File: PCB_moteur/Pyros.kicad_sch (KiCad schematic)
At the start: 51 parts, among them J1 Screw_Terminal_01x08, U12 SI5442DU-T1-GE3, U3 SI5442DU-T1-GE3, U6 LM339, U7 SI5442DU-T1-GE3

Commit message: wip: change 4 pyros -> 2 pyros
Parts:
- removed J1: Screw_Terminal_01x08, ODB:8pin_terminal_2mm54, symbol Connector:Screw_Terminal_01x08
- removed P_C4, P_C8: 22uF, Capacitor_SMD:C_0603_1608Metric, symbol Device:C_Small
- removed P_C5, P_C9: 0.1uF, Capacitor_SMD:C_0603_1608Metric, symbol Device:C_Small
- removed P_D3, P_D4, P_D7, P_D8: CDBQR0230R, Diode_SMD:D_SOD-923, symbol Diode:BAT54J
- removed P_R10, P_R18: 27k, Resistor_SMD:R_0603_1608Metric, symbol Device:R_Small
- removed P_R11, P_R19: 100, Resistor_SMD:R_0603_1608Metric, symbol Device:R_Small
- removed P_R12, P_R20: 3.3k, Resistor_SMD:R_0603_1608Metric, symbol Device:R_Small
- removed P_R17, P_R9: 180k, Resistor_SMD:R_0603_1608Metric, symbol Device:R_Small
- removed U12, U3: SI5442DU-T1-GE3, SON_8DU-T1-GE3_VIS, symbol ODB2:SI5442DU-T1-GE3
- removed U6: LM339, Package_SO:TSSOP-14_4.4x5mm_P0.65mm, symbol Comparator:LM339
- added J1: Screw_Terminal_01x04, symbol Connector:Screw_Terminal_01x04
- added U8: LM393, symbol Comparator:LM393
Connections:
- net +5V: now also U8.8 (V+)
- net Cmp_1: now also U8.1
- net Cmp_2: now also U8.7
- net GND: now also U8.4 (V-)
- net Pyro1-: now also J1.2 (Pin_2)
- net Pyro2-: now also J1.4 (Pin_4)
- net Vin_Pyro: now also J1.1 (Pin_1), J1.3 (Pin_3)
- net at P_R2.2, P_R4.1: now also U8.2 (-), U8.6 (-)
- net at P_R1.2, P_R3.1: now also U8.3 (+), U8.5 (+)
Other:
- note removed: "Pyro 3"
- note removed: "Pyro 4"
- moved on the sheet: P_C1

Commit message: fix: power supply + add LED RG + add mounting holes + change 6pins header SWD connector + pyros
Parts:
- P_C2, P_C7: value 0.1uF -> 100nF
- P_R1: value 24k 1% -> 102k 1%
- P_R13, P_R5: value 180k -> 39k
- P_R14, P_R6: value 27k -> 22k
- P_R15, P_R7: value 100 -> 100R
- P_R2: value 20k 1% -> 40k 1%
- P_R3: value 3.6k 1% -> 10k 1%
- P_R4: value 5k 1% -> 10k 1%
- Vin_R3: value 27K 1% -> 22K 1%
- Vin_R4: value 180k 1% -> 39k 1%
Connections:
- net +5V is gone; now on net +3V3: P_C1.1, U8.8 (V+)
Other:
- note added: "Power good protection, block the ignition if the power is not above 7.4v if V_{in} > 7.4 = Power good V_{ref} = 3.3 * R4 / (R2 + R4) = 0.66V if V_{in} = 7.4 * R3 / (R3 + R1) = 0.66v"
- note removed: "2 colors availabel for the connector 1715250000 : Black 1715310000 : Orange"
- note removed: "Power good protection, block the ignition if the power is not above 5.06v if V_{in} > 5.06 = Power good V_{ref} = ${/4b06c5d1-aa8b-48ed-8972-b43a60cfab78/8ab7427e-7183-4caa-ac8a-08b0bd412372/a7ab30b6-1c68-4176-964a-109ef5b035cc:VALUE} * ${/4b06c5d1-aa8b-48ed-8972-b43a60cfab78/8ab7427e-7183-4caa-ac8a-08b0bd412372/0614f46a-a67b-4246-947a-398bbcc78170:VALUE} / (${/4b06c5d1-aa8b-48ed-8972-b43a60cfab7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"
- moved on the sheet: J1, P_C2, P_C3, P_C6, P_C7, P_D1, P_D2, P_D5, P_D6, P_R13, P_R14, P_R15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

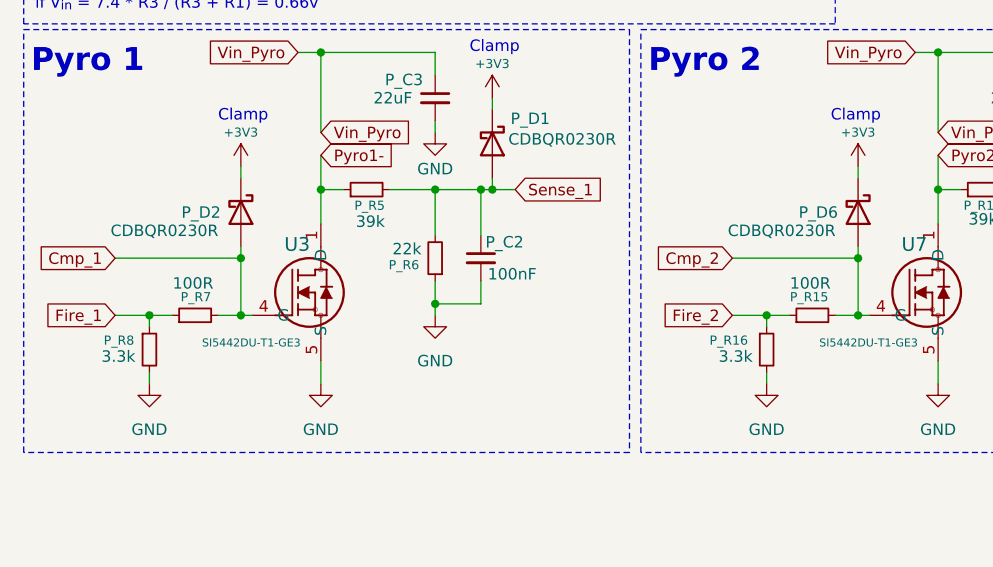
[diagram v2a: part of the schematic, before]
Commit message: fix: resistors + capacitances power supply
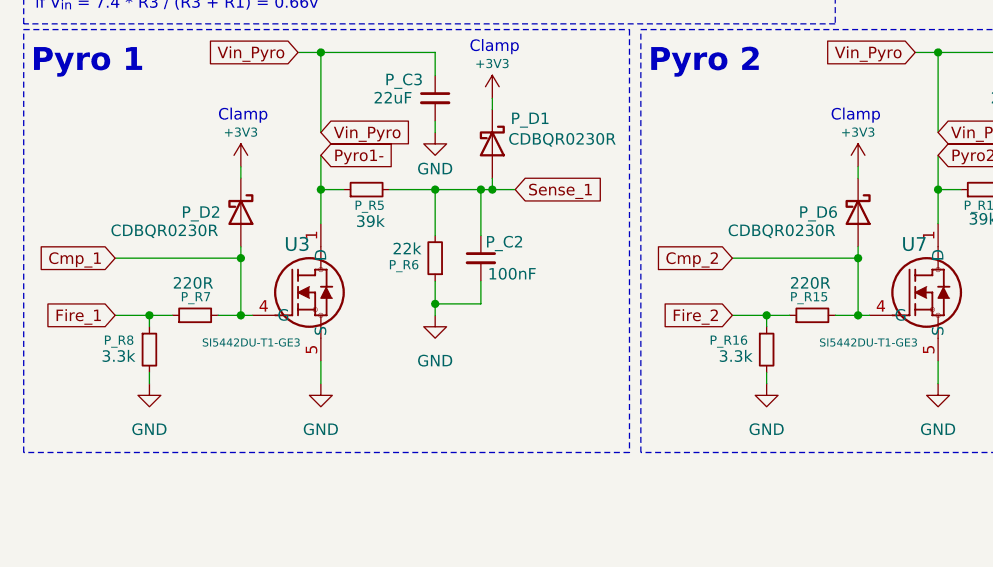
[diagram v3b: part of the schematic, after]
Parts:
- P_R15, P_R7: value 100R -> 220R
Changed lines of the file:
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@@
 			)
 		)
-		(property "Value" "100R"
+		(property "Value" "220R"
 			(at 103.632 112.014 90)
 			(effects
@@
 			)
 		)
-		(property "Value" "100R"
+		(property "Value" "220R"
 			(at 35.052 112.014 90)
 			(effects

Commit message: fix: pyros resistors + typos +
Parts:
- P_R15, P_R7: value 220R -> 1.5k
- P_R16, P_R8: value 3.3k -> 27k
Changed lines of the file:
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@@
 			)
 		)
-		(property "Value" "220R"
+		(property "Value" "1.5k"
 			(at 103.632 112.014 90)
 			(effects
@@
 			)
 		)
-		(property "Value" "3.3k"
+		(property "Value" "27k"
 			(at 22.606 120.142 0)
 			(effects
@@
 			)
 		)
-		(property "Value" "3.3k"
+		(property "Value" "27k"
 			(at 91.186 120.142 0)
 			(effects
@@
 			)
 		)
-		(property "Value" "220R"
+		(property "Value" "1.5k"
 			(at 35.052 112.014 90)
 			(effects

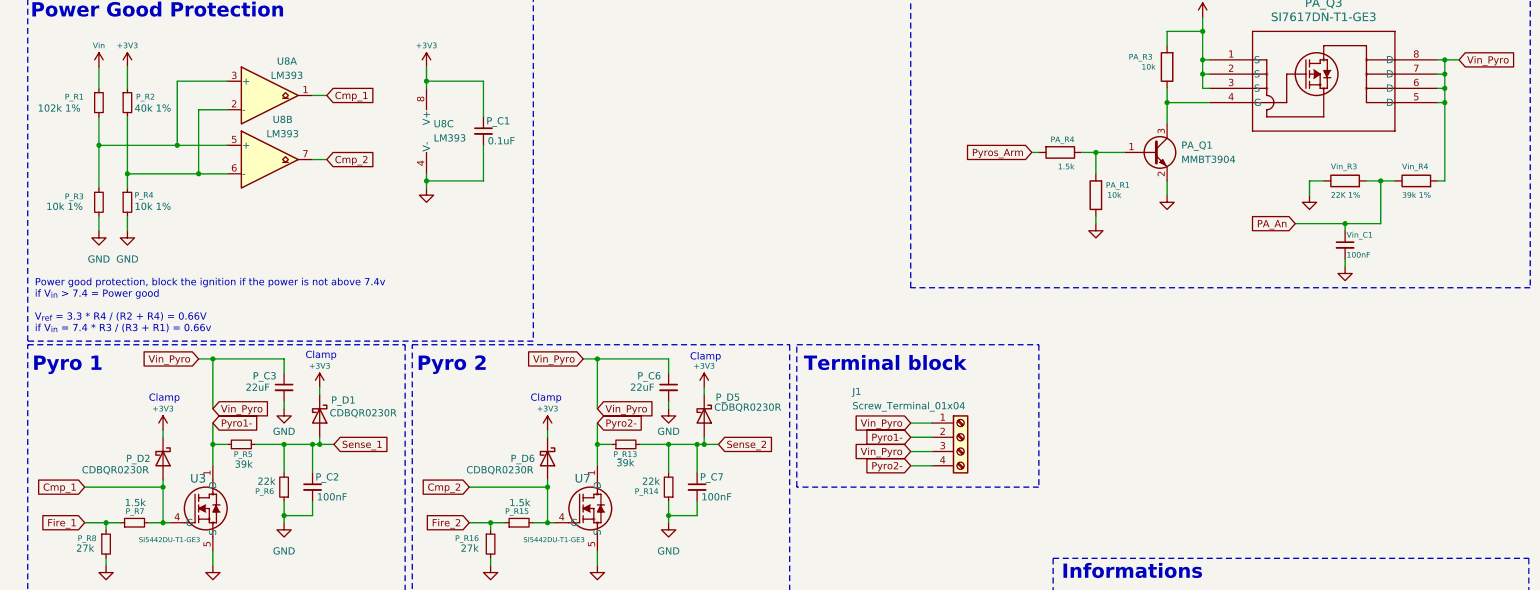
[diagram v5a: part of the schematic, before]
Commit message: fix: resistance ratios + typos
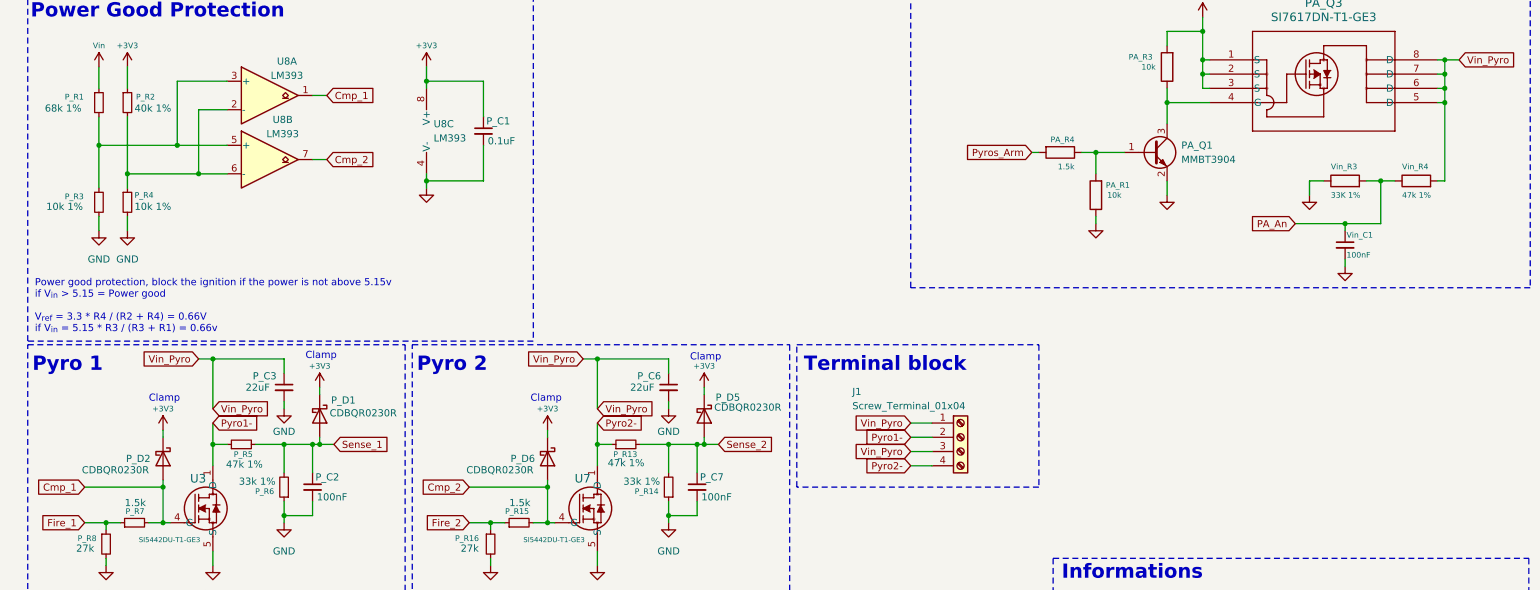
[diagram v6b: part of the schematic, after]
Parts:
- P_R1: value 102k 1% -> 68k 1%
- P_R13, P_R5: value 39k -> 47k 1%
- P_R14, P_R6: value 22k -> 33k 1%
- Vin_R3: value 22K 1% -> 33K 1%
- Vin_R4: value 39k 1% -> 47k 1%
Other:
- note added: "Power good protection, block the ignition if the power is not above 5.15v if V_{in} > 5.15 = Power good V_{ref} = 3.3 * R4 / (R2 + R4) = 0.66V if V_{in} = 5.15 * R3 / (R3 + R1) = 0.66v"
- note removed: "Power good protection, block the ignition if the power is not above 7.4v if V_{in} > 7.4 = Power good V_{ref} = 3.3 * R4 / (R2 + R4) = 0.66V if V_{in} = 7.4 * R3 / (R3 + R1) = 0.66v"
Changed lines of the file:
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@@
 		)
 	)
-	(text "Power good protection, block the ignition if the power is not above 7.4v\nif V_{in} > 7.4 = Power good\n\nV_{ref} = 3.3 * R4 / (R2 + R4) = 0.66V\nif V_{in} = 7.4 * R3 / (R3 + R1) = 0.66v\n"
+	(text "Power good protection, block the ignition if the power is not above 5.15v\nif V_{in} > 5.15 = Power good\n\nV_{ref} = 3.3 * R4 / (R2 + R4) = 0.66V\nif V_{in} = 5.15 * R3 / (R3 + R1) = 0.66v\n"
 		(exclude_from_sim no)
 		(at 15.24 76.962 0)
@@
 			)
 		)
-		(property "Value" "39k"
-			(at 54.102 105.156 90)
+		(property "Value" "47k 1%"
+			(at 55.88 105.156 90)
 			(effects
 				(font
@@
 			)
 		)
-		(property "Value" "22K 1%"
+		(property "Value" "33K 1%"
 			(at 246.38 57.15 90)
 			(effects
@@
 			)
 		)
-		(property "Value" "22k"
+		(property "Value" "33k 1%"
 			(at 58.166 108.204 0)
 			(effects
@@
 			)
 		)
-		(property "Value" "102k 1%"
-			(at 15.748 41.656 0)
+		(property "Value" "68k 1%"
+			(at 17.018 41.656 0)
 			(effects
 				(font
@@
 			)
 		)
-		(property "Value" "39k"
-			(at 122.174 104.902 90)
+		(property "Value" "47k 1%"
+			(at 123.952 104.902 90)
 			(effects
 				(font
@@
 			)
 		)
-		(property "Value" "39k 1%"
+		(property "Value" "47k 1%"
 			(at 259.08 57.15 90)
 			(effects
@@
 			)
 		)
-		(property "Value" "22k"
+		(property "Value" "33k 1%"
 			(at 126.746 108.204 0)
 			(effects
